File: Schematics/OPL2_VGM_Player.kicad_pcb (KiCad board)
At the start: 2 copper layers, 56.5 x 64.8 mm, 9 parts, among them J1 JACK, U1 Teensy3.5, U2 YM3812, U3 Y3014B, U4 LM358N, X1 3.579545MHz

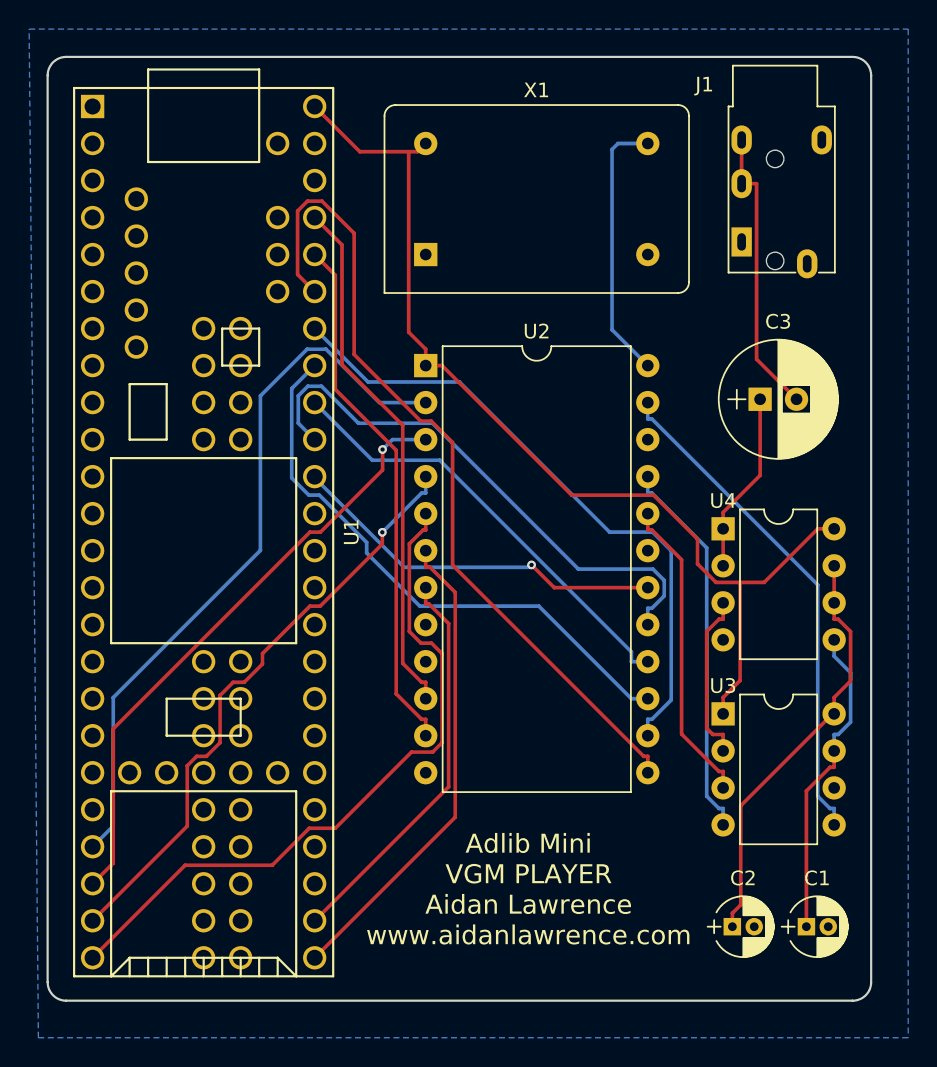
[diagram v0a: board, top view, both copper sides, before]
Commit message: Updated schematics and PCB to support playback buttons.
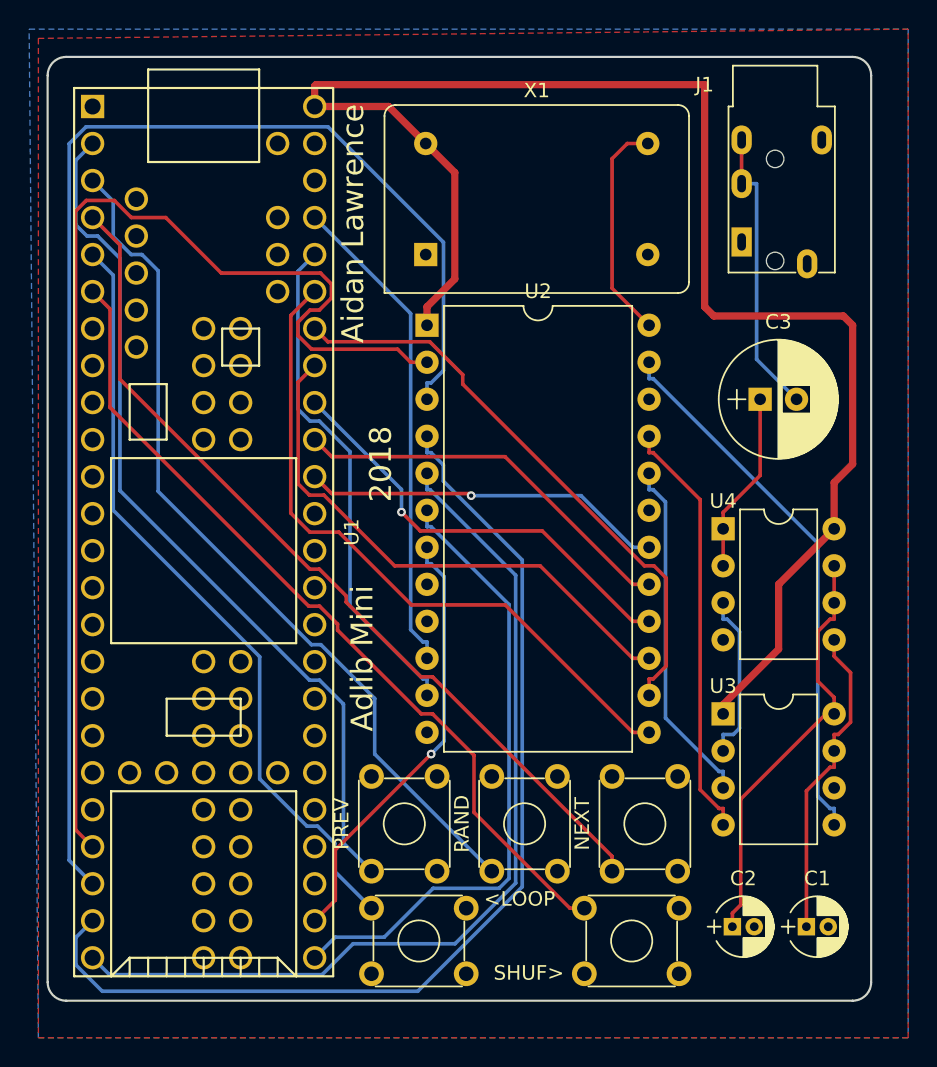
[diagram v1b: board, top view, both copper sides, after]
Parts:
- added <LOOP: LOOP, Buttons_Switches_THT:SW_TH_Tactile_Omron_B3F-10xx, F.Cu at (142.9, 136.5)
- added NEXT: NEXT, Buttons_Switches_THT:SW_TH_Tactile_Omron_B3F-10xx, F.Cu at (159.4, 134.0)
- added PREV: PREV, Buttons_Switches_THT:SW_TH_Tactile_Omron_B3F-10xx, F.Cu at (142.9, 134.0)
- added RAND: RAND, Buttons_Switches_THT:SW_TH_Tactile_Omron_B3F-10xx, F.Cu at (151.1, 134.0)
- added SHUF>: SHUF, Buttons_Switches_THT:SW_TH_Tactile_Omron_B3F-10xx, F.Cu at (157.5, 136.5)
- J1: value JACK -> JACK_TRS_6PINS
- moved U2 2.77 mm to (146.7, 96.5)
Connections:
- U1 pad 2: Net-(U1-Pad2) -> PREV
- U1 pad 3: Net-(U1-Pad3) -> RAND
- U1 pad 4: Net-(U1-Pad4) -> NEXT
- U1 pad 5: Net-(U1-Pad5) -> LOOP
- U1 pad 6: Net-(U1-Pad6) -> SHUF
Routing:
- net NEXT: track 0.00 -> 60.5 mm
- net PREV: track 0.00 -> 59.7 mm
- net RAND: track 0.00 -> 59.6 mm
- net SHUF: track 0.00 -> 57.8 mm
- net LOOP: track 0.00 -> 53.2 mm
- net YM_IC: track 41.7 -> 92.3 mm, vias 1 -> 0
- net +5V: track 70.5 -> 107.2 mm
- net YM_A0: track 41.4 -> 71.6 mm, vias 1 -> 0
- net YM_IRQ: track 49.9 -> 78.8 mm
- net YM_WR: track 47.7 -> 62.9 mm
- net D6: track 38.0 -> 27.1 mm
- net YM_RD: track 32.9 -> 43.4 mm
- net D2: track 57.0 -> 46.7 mm
- net D3: track 44.3 -> 40.3 mm
- net Net-(U2-Pad24): track 18.5 -> 15.4 mm
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- added copper zone on F.Cu, net GND
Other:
- net class +5v added: clearance 0.2, trace_width 0.5, via_dia 0.6, via_drill 0.4
- board text added: "2018"
- board text added: "Adlib Mini"
- board text added: "Aidan Lawrence"

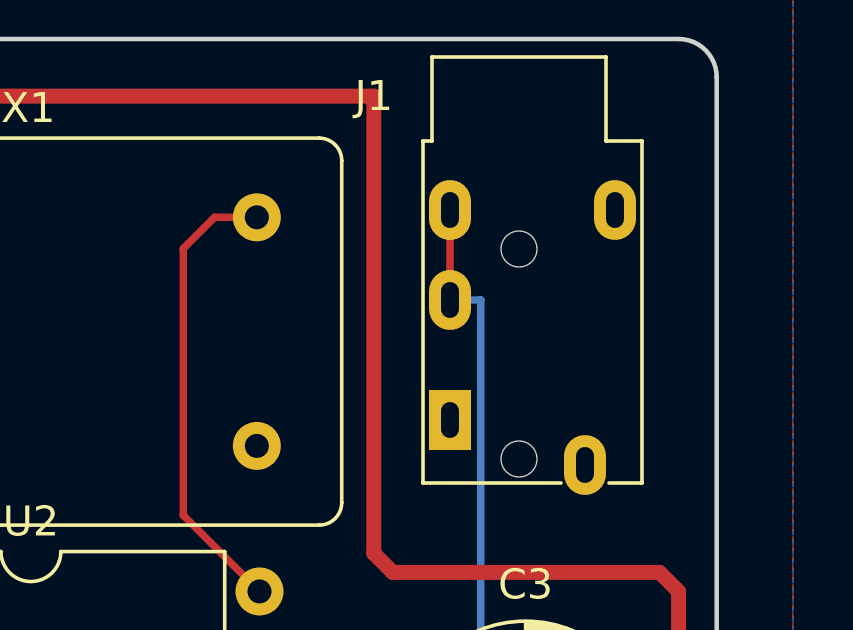
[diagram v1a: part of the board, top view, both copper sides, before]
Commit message: Fixed jack GND on board and schematic. Added control button support
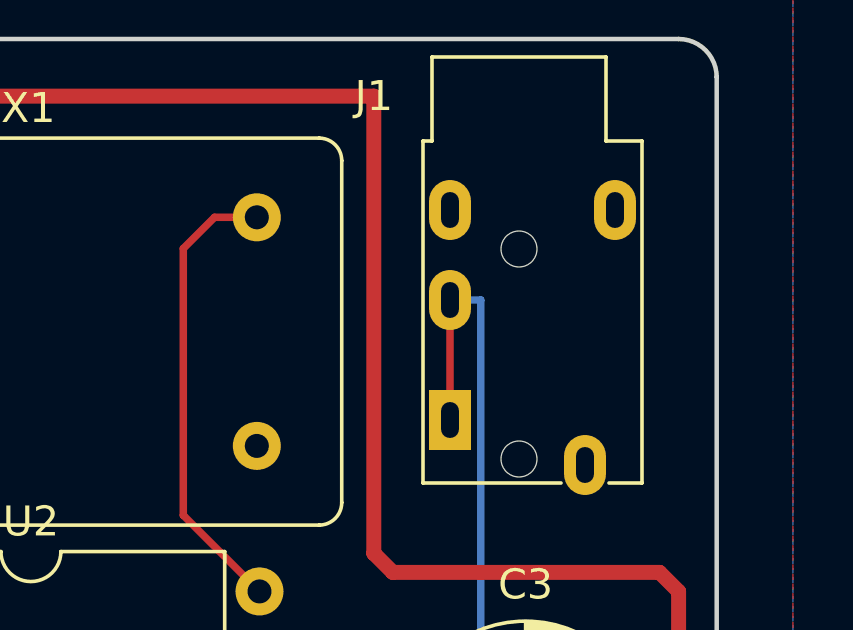
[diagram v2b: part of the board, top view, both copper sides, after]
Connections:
- J1 pad 1: GND -> Net-(C3-Pad2)
- J1 pad 3: Net-(C3-Pad2) -> GND
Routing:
- net Net-(C3-Pad2): track 20.0 -> 21.0 mm
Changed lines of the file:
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@@
-(kicad_pcb (version 4) (host pcbnew 4.0.6)
+(kicad_pcb (version 4) (host pcbnew 4.0.7)
   (general
     (links 53)
@@
     (0 F.Cu signal)
     (31 B.Cu signal)
-    (32 B.Adhes user)
-    (33 F.Adhes user)
-    (34 B.Paste user)
-    (35 F.Paste user)
-    (36 B.SilkS user)
-    (37 F.SilkS user)
-    (38 B.Mask user)
-    (39 F.Mask user)
-    (40 Dwgs.User user)
-    (41 Cmts.User user)
-    (42 Eco1.User user)
-    (43 Eco2.User user)
-    (44 Edge.Cuts user)
-    (45 Margin user)
-    (46 B.CrtYd user)
-    (47 F.CrtYd user)
-    (48 B.Fab user)
-    (49 F.Fab user)
+    (32 B.Adhes user hide)
+    (33 F.Adhes user hide)
+    (34 B.Paste user hide)
+    (35 F.Paste user hide)
+    (36 B.SilkS user hide)
+    (37 F.SilkS user hide)
+    (38 B.Mask user hide)
+    (39 F.Mask user hide)
+    (40 Dwgs.User user hide)
+    (41 Cmts.User user hide)
+    (42 Eco1.User user hide)
+    (43 Eco2.User user hide)
+    (44 Edge.Cuts user hide)
+    (45 Margin user hide)
+    (46 B.CrtYd user hide)
+    (47 F.CrtYd user hide)
+    (48 B.Fab user hide)
+    (49 F.Fab user hide)
   )
   (setup
@@
     (mod_text_size 1 1)
     (mod_text_width 0.15)
-    (pad_size 1.524 1.524)
-    (pad_drill 0.762)
+    (pad_size 2 1.4)
+    (pad_drill 1.2)
     (pad_to_mask_clearance 0.2)
     (aux_axis_origin 0 0)
@@
       (net 7 "Net-(J1-Pad4)"))
     (pad 1 thru_hole rect (at 0 0 270) (size 2 1.4) (drill oval 1.2 0.6) (layers *.Cu *.Mask)
-      (net 2 GND))
+      (net 5 "Net-(C3-Pad2)"))
     (pad 2 thru_hole oval (at 0 -4 270) (size 2 1.4) (drill oval 1.2 0.6) (layers *.Cu *.Mask)
       (net 5 "Net-(C3-Pad2)"))
     (pad 3 thru_hole oval (at 0 -7 270) (size 2 1.4) (drill oval 1.2 0.6) (layers *.Cu *.Mask)
-      (net 5 "Net-(C3-Pad2)"))
+      (net 2 GND))
     (pad "" np_thru_hole circle (at 2.3 -5.7 270) (size 1.2 1.2) (drill 1.2) (layers *.Cu *.Mask))
     (pad "" np_thru_hole circle (at 2.3 1.3 270) (size 1.2 1.2) (drill 1.2) (layers *.Cu *.Mask))
@@
   (segment (start 167.005 109.3647) (end 169.545 106.8247) (width 0.25) (layer F.Cu) (net 4))
   (segment (start 167.005 110.49) (end 167.005 109.3647) (width 0.25) (layer F.Cu) (net 4))
-  (segment (start 168.275 83.805) (end 168.275 86.805) (width 0.25) (layer F.Cu) (net 5))
+  (segment (start 168.275 86.805) (end 168.275 90.805) (width 0.25) (layer F.Cu) (net 5) (status C00000))
   (segment (start 169.3003 98.8553) (end 172.045 101.6) (width 0.25) (layer B.Cu) (net 5))
   (segment (start 169.3003 86.805) (end 169.3003 98.8553) (width 0.25) (layer B.Cu) (net 5))
